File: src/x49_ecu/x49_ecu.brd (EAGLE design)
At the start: 165.1 x 101.6 mm, 16 parts, among them J1 1-776163-4, J2 DTP13-4P, J3 DTP13-4P

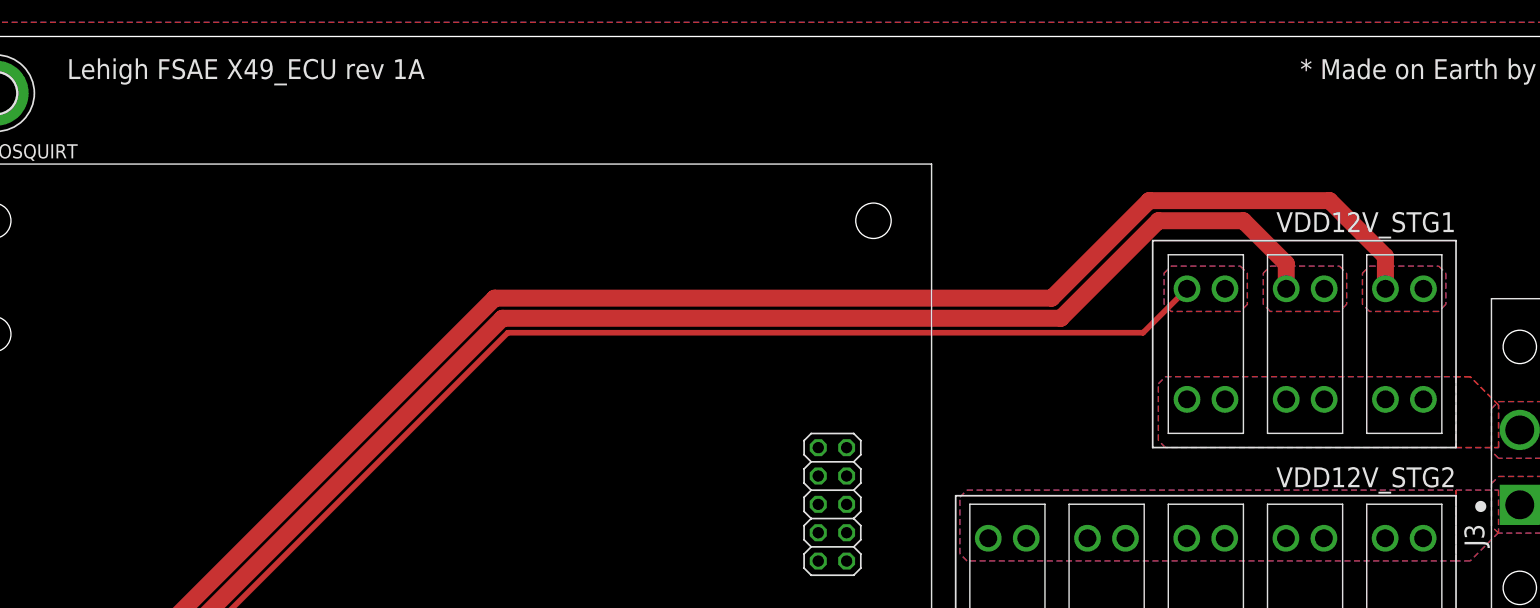
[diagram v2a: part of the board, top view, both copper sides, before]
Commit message: x49_ecu: 1C with status LEDs
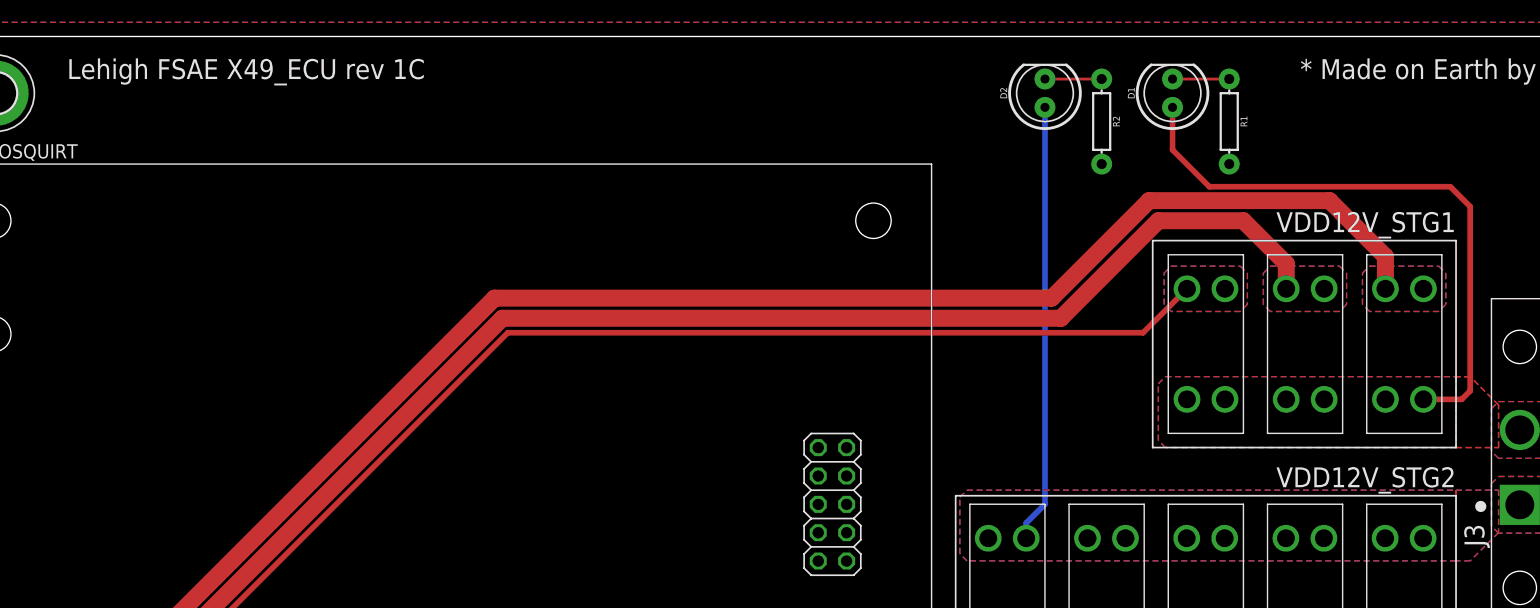
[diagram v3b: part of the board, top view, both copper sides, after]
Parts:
- added D1, D2: 560, SparkFun-LED:LED_5MM
- added R1, R2: (no value), SparkFun-Resistors:AXIAL-0.3
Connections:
- new net N$1: D1.K, R1.P$1
- new net N$2: D2.K, R2.P$1
- net GND: now also R1.P$2, R2.P$2
- net VDD12V_STG1: now also D1.A
- net VDD12V_STG2: now also D2.A
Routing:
- net VDD12V_STG1: track 0.00 -> 53.6 mm
- net VDD12V_STG2: track 0.00 -> 39.3 mm
- net N$2: track 0.00 -> 5.08 mm
- net N$1: track 0.00 -> 5.08 mm
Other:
- board text added: "Lehigh FSAE X49_ECU rev 1C"
- board text removed: "Lehigh FSAE X49_ECU rev 1A"
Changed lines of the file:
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@@
 <layer number="230" name="230bmp" color="7" fill="1" visible="yes" active="yes"/>
 <layer number="231" name="231bmp" color="7" fill="1" visible="yes" active="yes"/>
+<layer number="232" name="Eagle3D_PG2" color="7" fill="1" visible="yes" active="yes"/>
+<layer number="233" name="Eagle3D_PG3" color="7" fill="1" visible="yes" active="yes"/>
 <layer number="248" name="Housing" color="7" fill="1" visible="yes" active="yes"/>
 <layer number="249" name="Edge" color="7" fill="1" visible="yes" active="yes"/>
@@
 <wire x1="135.89" y1="64.77" x2="108.712" y2="64.77" width="0.1524" layer="21"/>
 <wire x1="108.712" y1="64.77" x2="108.712" y2="83.312" width="0.1524" layer="21"/>
-<text x="11.43" y="97.79" size="1.778" layer="21">Lehigh FSAE X49_ECU rev 1A</text>
+<text x="11.43" y="97.79" size="1.778" layer="21">Lehigh FSAE X49_ECU rev 1C</text>
 </plain>
 <attributes>
@@
 <element name="U$8" library="keystone_electronics" package="3568" value="3568" x="102.87" y="56.642" smashed="yes" rot="R270"/>
 <element name="U$9" library="keystone_electronics" package="3568" value="3568" x="129.54" y="56.642" smashed="yes" rot="R270"/>
+<element name="D1" library="SparkFun-LED" library_urn="urn:adsk.eagle:library:529" package="LED_5MM" package3d_urn="urn:adsk.eagle:package:39353/1" value="560" x="110.49" y="96.52" smashed="yes" rot="R90">
+<attribute name="NAME" x="107.0991" y="96.52" size="0.6096" layer="25" font="vector" ratio="20" rot="R90" align="bottom-center"/>
+<attribute name="VALUE" x="113.8809" y="96.5454" size="0.6096" layer="27" font="vector" ratio="20" rot="R90" align="top-center"/>
+</element>
+<element name="D2" library="SparkFun-LED" library_urn="urn:adsk.eagle:library:529" package="LED_5MM" package3d_urn="urn:adsk.eagle:package:39353/1" value="560" x="99.06" y="96.52" smashed="yes" rot="R90">
+<attribute name="NAME" x="95.6691" y="96.52" size="0.6096" layer="25" font="vector" ratio="20" rot="R90" align="bottom-center"/>
+<attribute name="VALUE" x="102.4509" y="96.5454" size="0.6096" layer="27" font="vector" ratio="20" rot="R90" align="top-center"/>
+</element>
+<element name="R1" library="SparkFun-Resistors" library_urn="urn:adsk.eagle:library:532" package="AXIAL-0.3" package3d_urn="urn:adsk.eagle:package:39658/1" value=" " x="115.57" y="93.98" smashed="yes" rot="R270">
+<attribute name="NAME" x="116.586" y="93.98" size="0.6096" layer="25" font="vector" ratio="20" rot="R270" align="bottom-center"/>
+<attribute name="PROD_ID" value=" " x="115.57" y="93.98" size="1.778" layer="27" rot="R270" display="off"/>
+<attribute name="VALUE" x="114.554" y="93.98" size="0.6096" layer="27" font="vector" ratio="20" rot="R270" align="top-center"/>
+</element>
+<element name="R2" library="SparkFun-Resistors" library_urn="urn:adsk.eagle:library:532" package="AXIAL-0.3" package3d_urn="urn:adsk.eagle:package:39658/1" value=" " x="104.14" y="93.98" smashed="yes" rot="R270">
+<attribute name="NAME" x="105.156" y="93.98" size="0.6096" layer="25" font="vector" ratio="20" rot="R270" align="bottom-center"/>
+<attribute name="PROD_ID" value=" " x="104.14" y="93.98" size="1.778" layer="27" rot="R270" display="off"/>
+<attribute name="VALUE" x="103.124" y="93.98" size="0.6096" layer="27" font="vector" ratio="20" rot="R270" align="top-center"/>
+</element>
 </elements>
 <signals>
@@
 <contactref element="J3" pad="3"/>
 <contactref element="J3" pad="4"/>
+<contactref element="R2" pad="P$2"/>
+<contactref element="R1" pad="P$2"/>
 </signal>
 <signal name="VDD12V_STG2" class="1">
@@
 <vertex x="135.89" y="60.96"/>
 </polygon>
+<contactref element="D2" pad="A"/>
+<wire x1="99.06" y1="95.25" x2="99.06" y2="59.69" width="0.508" layer="16"/>
+<wire x1="99.06" y1="59.69" x2="97.3836" y2="58.0136" width="0.508" layer="16"/>
+<wire x1="97.3836" y1="58.0136" x2="97.3836" y2="56.642" width="0.508" layer="16"/>
 </signal>
 <signal name="VDD12V_IGN_INJ" class="1">
@@
 <vertex x="135.89" y="71.12"/>
 </polygon>
+<contactref element="D1" pad="A"/>
+<wire x1="110.49" y1="95.25" x2="110.49" y2="91.44" width="0.508" layer="1"/>
+<wire x1="135.382" y1="88.138" x2="137.16" y2="86.36" width="0.508" layer="1"/>
+<wire x1="137.16" y1="86.36" x2="137.16" y2="69.85" width="0.508" layer="1"/>
+<wire x1="110.49" y1="91.44" x2="113.792" y2="88.138" width="0.508" layer="1"/>
+<wire x1="113.792" y1="88.138" x2="135.382" y2="88.138" width="0.508" layer="1"/>
+<wire x1="137.16" y1="69.85" x2="136.398" y2="69.088" width="0.508" layer="1"/>
+<wire x1="136.398" y1="69.088" x2="132.969" y2="69.088" width="0.508" layer="1"/>
 </signal>
 <signal name="CAN_H">
@@
 <signal name="VDD12V_STG6" class="1">
 </signal>
+<signal name="N$1">
+<contactref element="D1" pad="K"/>
+<contactref element="R1" pad="P$1"/>
+<wire x1="110.49" y1="97.79" x2="115.57" y2="97.79" width="0.254" layer="1"/>
+</signal>
+<signal name="N$2">
+<contactref element="D2" pad="K"/>
+<contactref element="R2" pad="P$1"/>
+<wire x1="99.06" y1="97.79" x2="104.14" y2="97.79" width="0.254" layer="1"/>
+</signal>
 </signals>

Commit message: x49_ecu: Rev 1D
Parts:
- moved D2 2.54 mm to (96.5, 96.5)
- moved R2 2.54 mm to (101.6, 94.0)
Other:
- board text added: "Lehigh FSAE X49_ECU rev 1D"
- board text added: "STG1"
- board text added: "STG2"
- board text removed: "Lehigh FSAE X49_ECU rev 1C"
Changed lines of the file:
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@@
 <wire x1="135.89" y1="64.77" x2="108.712" y2="64.77" width="0.1524" layer="21"/>
 <wire x1="108.712" y1="64.77" x2="108.712" y2="83.312" width="0.1524" layer="21"/>
-<text x="11.43" y="97.79" size="1.778" layer="21">Lehigh FSAE X49_ECU rev 1C</text>
+<text x="11.43" y="97.79" size="1.778" layer="21">Lehigh FSAE X49_ECU rev 1D</text>
+<text x="106.68" y="90.17" size="1.778" layer="21">STG1</text>
+<text x="92.71" y="90.17" size="1.778" layer="21">STG2</text>
 </plain>
 <attributes>
@@
 <element name="D1" library="SparkFun-LED" library_urn="urn:adsk.eagle:library:529" package="LED_5MM" package3d_urn="urn:adsk.eagle:package:39353/1" value="560" x="110.49" y="96.52" smashed="yes" rot="R90">
 <attribute name="NAME" x="107.0991" y="96.52" size="0.6096" layer="25" font="vector" ratio="20" rot="R90" align="bottom-center"/>
-<attribute name="VALUE" x="113.8809" y="96.5454" size="0.6096" layer="27" font="vector" ratio="20" rot="R90" align="top-center"/>
+<attribute name="VALUE" x="113.8809" y="94.0054" size="0.6096" layer="27" font="vector" ratio="20" rot="R90" align="top-center"/>
 </element>
-<element name="D2" library="SparkFun-LED" library_urn="urn:adsk.eagle:library:529" package="LED_5MM" package3d_urn="urn:adsk.eagle:package:39353/1" value="560" x="99.06" y="96.52" smashed="yes" rot="R90">
-<attribute name="NAME" x="95.6691" y="96.52" size="0.6096" layer="25" font="vector" ratio="20" rot="R90" align="bottom-center"/>
-<attribute name="VALUE" x="102.4509" y="96.5454" size="0.6096" layer="27" font="vector" ratio="20" rot="R90" align="top-center"/>
+<element name="D2" library="SparkFun-LED" library_urn="urn:adsk.eagle:library:529" package="LED_5MM" package3d_urn="urn:adsk.eagle:package:39353/1" value="560" x="96.52" y="96.52" smashed="yes" rot="R90">
+<attribute name="NAME" x="93.1291" y="96.52" size="0.6096" layer="25" font="vector" ratio="20" rot="R90" align="bottom-center"/>
+<attribute name="VALUE" x="99.9109" y="94.0054" size="0.6096" layer="27" font="vector" ratio="20" rot="R90" align="top-center"/>
 </element>
 <element name="R1" library="SparkFun-Resistors" library_urn="urn:adsk.eagle:library:532" package="AXIAL-0.3" package3d_urn="urn:adsk.eagle:package:39658/1" value=" " x="115.57" y="93.98" smashed="yes" rot="R270">
@@
 <attribute name="VALUE" x="114.554" y="93.98" size="0.6096" layer="27" font="vector" ratio="20" rot="R270" align="top-center"/>
 </element>
-<element name="R2" library="SparkFun-Resistors" library_urn="urn:adsk.eagle:library:532" package="AXIAL-0.3" package3d_urn="urn:adsk.eagle:package:39658/1" value=" " x="104.14" y="93.98" smashed="yes" rot="R270">
-<attribute name="NAME" x="105.156" y="93.98" size="0.6096" layer="25" font="vector" ratio="20" rot="R270" align="bottom-center"/>
-<attribute name="PROD_ID" value=" " x="104.14" y="93.98" size="1.778" layer="27" rot="R270" display="off"/>
-<attribute name="VALUE" x="103.124" y="93.98" size="0.6096" layer="27" font="vector" ratio="20" rot="R270" align="top-center"/>
+<element name="R2" library="SparkFun-Resistors" library_urn="urn:adsk.eagle:library:532" package="AXIAL-0.3" package3d_urn="urn:adsk.eagle:package:39658/1" value=" " x="101.6" y="93.98" smashed="yes" rot="R270">
+<attribute name="NAME" x="102.616" y="93.98" size="0.6096" layer="25" font="vector" ratio="20" rot="R270" align="bottom-center"/>
+<attribute name="PROD_ID" value=" " x="101.6" y="93.98" size="1.778" layer="27" rot="R270" display="off"/>
+<attribute name="VALUE" x="100.584" y="93.98" size="0.6096" layer="27" font="vector" ratio="20" rot="R270" align="top-center"/>
 </element>
 </elements>
@@
 </polygon>
 <contactref element="D2" pad="A"/>
-<wire x1="99.06" y1="95.25" x2="99.06" y2="59.69" width="0.508" layer="16"/>
-<wire x1="99.06" y1="59.69" x2="97.3836" y2="58.0136" width="0.508" layer="16"/>
-<wire x1="97.3836" y1="58.0136" x2="97.3836" y2="56.642" width="0.508" layer="16"/>
+<wire x1="96.52" y1="95.25" x2="96.52" y2="57.5056" width="0.508" layer="16"/>
+<wire x1="96.52" y1="57.5056" x2="97.3836" y2="56.642" width="0.508" layer="16"/>
 </signal>
 <signal name="VDD12V_IGN_INJ" class="1">
@@
 <contactref element="D2" pad="K"/>
 <contactref element="R2" pad="P$1"/>
-<wire x1="99.06" y1="97.79" x2="104.14" y2="97.79" width="0.254" layer="1"/>
+<wire x1="96.52" y1="97.79" x2="101.6" y2="97.79" width="0.254" layer="1"/>
 </signal>
 </signals>

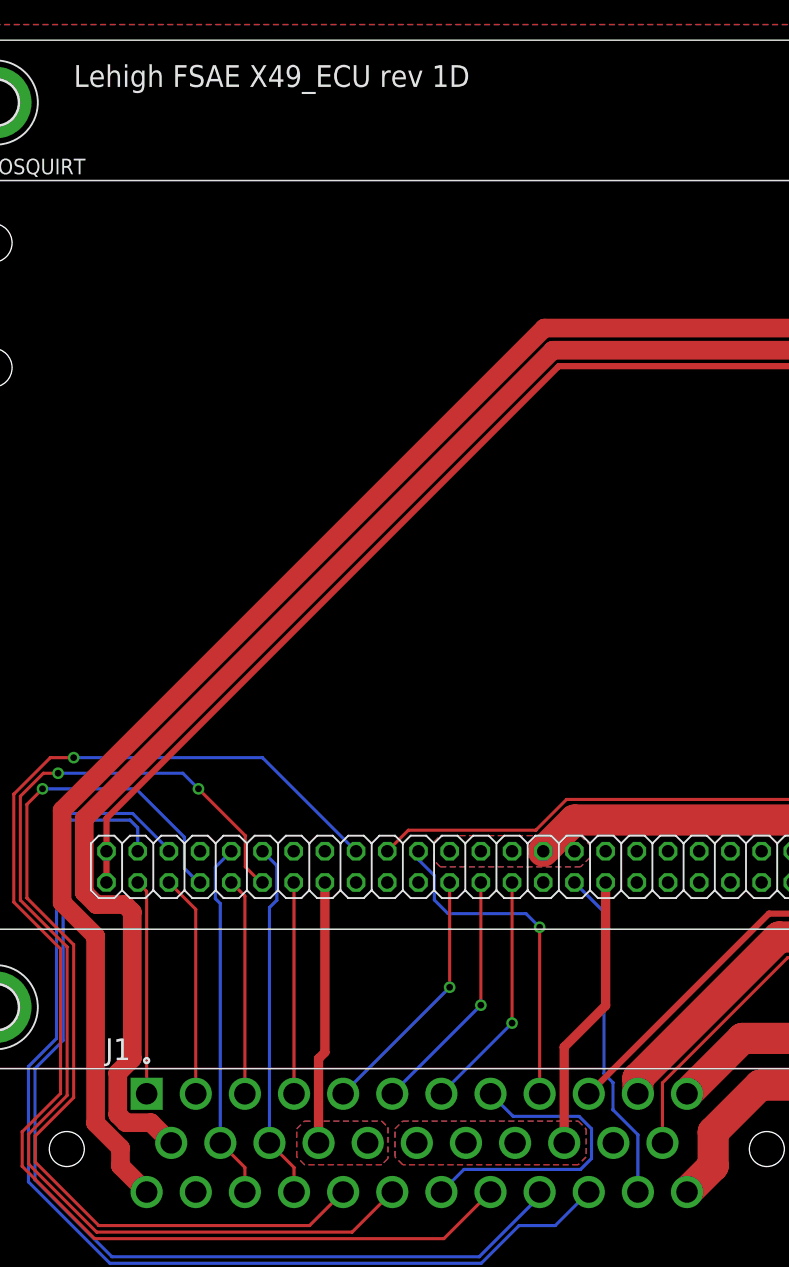
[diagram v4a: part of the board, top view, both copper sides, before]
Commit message: x49_ecu: Rev 1E with fixed O2 sensor gnd
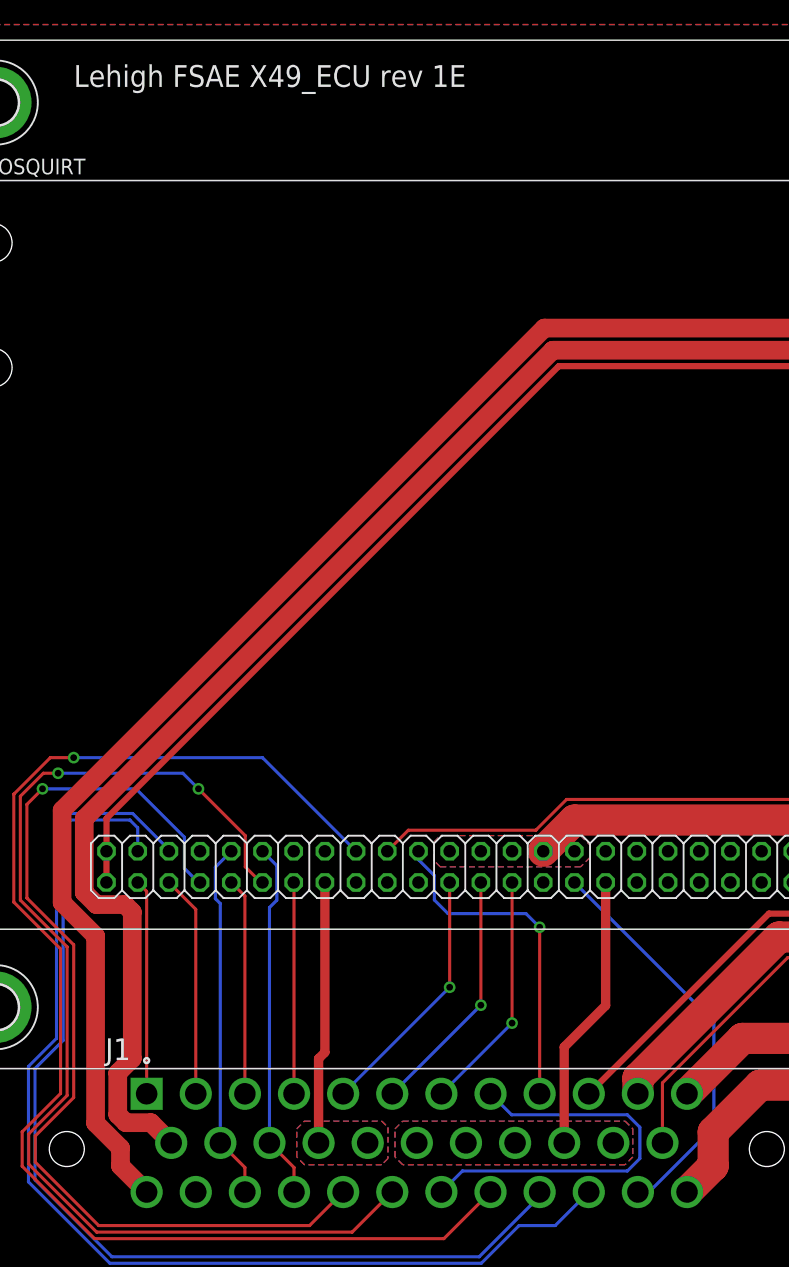
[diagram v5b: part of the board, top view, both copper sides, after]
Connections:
- net GND: no longer J1.22
- net SENSOR_GND: now also J1.22
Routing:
- net NEUTRAL_IN: track 25.2 -> 33.1 mm
- net SERIAL_GND: track 27.3 -> 33.0 mm
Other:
- board text added: "Lehigh FSAE X49_ECU rev 1E"
- board text removed: "Lehigh FSAE X49_ECU rev 1D"
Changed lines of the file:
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@@
 <?xml version="1.0" encoding="utf-8"?>
 <!DOCTYPE eagle SYSTEM "eagle.dtd">
-<eagle version="9.3.0">
+<eagle version="9.3.1">
 <drawing>
 <settings>
@@
 <wire x1="135.89" y1="64.77" x2="108.712" y2="64.77" width="0.1524" layer="21"/>
 <wire x1="108.712" y1="64.77" x2="108.712" y2="83.312" width="0.1524" layer="21"/>
-<text x="11.43" y="97.79" size="1.778" layer="21">Lehigh FSAE X49_ECU rev 1D</text>
+<text x="11.43" y="97.79" size="1.778" layer="21">Lehigh FSAE X49_ECU rev 1E</text>
 <text x="106.68" y="90.17" size="1.778" layer="21">STG1</text>
 <text x="92.71" y="90.17" size="1.778" layer="21">STG2</text>
@@
 <contactref element="H1" pad="B3,6"/>
 <contactref element="J1" pad="25"/>
-<contactref element="J1" pad="22"/>
 <contactref element="J3" pad="3"/>
 <contactref element="J3" pad="4"/>
@@
 <polygon width="0.254" layer="1">
 <vertex x="38.227" y="13.589"/>
-<vertex x="52.5145" y="13.589"/>
-<vertex x="53.1495" y="12.954"/>
-<vertex x="53.1495" y="10.668"/>
-<vertex x="52.5145" y="10.033"/>
+<vertex x="56.3245" y="13.589"/>
+<vertex x="56.9595" y="12.954"/>
+<vertex x="56.9595" y="10.668"/>
+<vertex x="56.3245" y="10.033"/>
 <vertex x="38.227" y="10.033"/>
 <vertex x="37.592" y="10.668"/>
@@
 <polygon width="0.254" layer="16">
 <vertex x="38.227" y="13.589"/>
-<vertex x="52.5145" y="13.589"/>
-<vertex x="53.1495" y="12.954"/>
-<vertex x="53.1495" y="10.668"/>
-<vertex x="52.5145" y="10.033"/>
+<vertex x="56.3245" y="13.589"/>
+<vertex x="56.9595" y="12.954"/>
+<vertex x="56.9595" y="10.668"/>
+<vertex x="56.3245" y="10.033"/>
 <vertex x="38.227" y="10.033"/>
 <vertex x="37.592" y="10.668"/>
@@
 <wire x1="54.743" y1="22.993" x2="54.743" y2="33.0172" width="0.762" layer="1"/>
 <wire x1="51.37" y1="19.62" x2="54.743" y2="22.993" width="0.762" layer="1"/>
+<contactref element="J1" pad="22"/>
 </signal>
 <signal name="VDD12V_DASH" class="1">
@@
 <contactref element="J1" pad="8"/>
 <contactref element="J1" pad="30"/>
-<wire x1="41.37" y1="7.811" x2="43.211" y2="9.652" width="0.254" layer="16"/>
-<wire x1="52.705" y1="9.652" x2="53.594" y2="10.541" width="0.254" layer="16"/>
-<wire x1="53.594" y1="12.954" x2="52.578" y2="13.97" width="0.254" layer="16"/>
-<wire x1="52.578" y1="13.97" x2="47.211" y2="13.97" width="0.254" layer="16"/>
-<wire x1="47.211" y1="13.97" x2="45.37" y2="15.811" width="0.254" layer="16"/>
-<wire x1="43.211" y1="9.652" x2="52.705" y2="9.652" width="0.254" layer="16"/>
-<wire x1="53.594" y1="10.541" x2="53.594" y2="12.954" width="0.254" layer="16"/>
+<wire x1="41.37" y1="7.811" x2="43.084" y2="9.525" width="0.254" layer="16"/>
+<wire x1="56.515" y1="9.525" x2="57.531" y2="10.541" width="0.254" layer="16"/>
+<wire x1="57.531" y1="13.081" x2="56.515" y2="14.097" width="0.254" layer="16"/>
+<wire x1="56.515" y1="14.097" x2="47.084" y2="14.097" width="0.254" layer="16"/>
+<wire x1="47.084" y1="14.097" x2="45.37" y2="15.811" width="0.254" layer="16"/>
+<wire x1="43.084" y1="9.525" x2="56.515" y2="9.525" width="0.254" layer="16"/>
+<wire x1="57.531" y1="10.541" x2="57.531" y2="13.081" width="0.254" layer="16"/>
 </signal>
 <signal name="FAN_EN_OUT">
@@
 <contactref element="MICROSQUIRT" pad="SERIAL_GND"/>
 <contactref element="J1" pad="34"/>
-<wire x1="57.37" y1="7.811" x2="57.37" y2="12.48" width="0.254" layer="16"/>
-<wire x1="55.3429" y1="16.7243875" x2="54.61" y2="17.4572875" width="0.254" layer="16"/>
-<wire x1="55.3429" y1="14.5071" x2="55.3429" y2="16.7243875" width="0.254" layer="16"/>
-<wire x1="57.37" y1="12.48" x2="55.3429" y2="14.5071" width="0.254" layer="16"/>
-<wire x1="54.61" y1="30.6102" x2="52.203" y2="33.0172" width="0.254" layer="16"/>
-<wire x1="54.61" y1="17.4572875" x2="54.61" y2="30.6102" width="0.254" layer="16"/>
+<wire x1="63.5545" y1="13.0875" x2="58.278" y2="7.811" width="0.254" layer="16"/>
+<wire x1="58.278" y1="7.811" x2="57.37" y2="7.811" width="0.254" layer="16"/>
+<wire x1="63.5545" y1="13.0875" x2="63.5545" y2="21.6657" width="0.254" layer="16"/>
+<wire x1="63.5545" y1="21.6657" x2="52.203" y2="33.0172" width="0.254" layer="16"/>
 </signal>
 <signal name="VDD12V_STG6" class="1">
